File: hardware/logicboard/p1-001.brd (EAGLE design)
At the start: 47 x 72 mm, 24 parts, among them IC1 74LS07N

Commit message: OSHW logo.
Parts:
- added LOGO2: OSHW-LOGOL-COPPER, SparkFun-Aesthetics:OSHW-LOGO-L_COPPER
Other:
- board text removed: "/"
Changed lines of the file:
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@@
 <wire x1="16" y1="65" x2="16" y2="57" width="0.1524" layer="21"/>
 <wire x1="16" y1="57" x2="15" y2="57" width="0.1524" layer="21"/>
-<text x="6" y="61" size="5.08" layer="25" align="center">/</text>
 <text x="26.67" y="69.85" size="0.8128" layer="25" rot="R180" align="center">D4</text>
 <text x="29.21" y="69.85" size="0.8128" layer="25" rot="R180" align="center">D5</text>
@@
 <attribute name="VALUE" x="28.702" y="65.659" size="0.6096" layer="27" font="vector" ratio="20"/>
 </element>
+<element name="LOGO2" library="SparkFun-Aesthetics" package="OSHW-LOGO-L_COPPER" value="OSHW-LOGOL-COPPER" x="6" y="61"/>
 </elements>
 <signals>

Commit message: Pineapple logo v2.
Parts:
- removed LOGO2: OSHW-LOGOL-COPPER, SparkFun-Aesthetics:OSHW-LOGO-L_COPPER
- added LOGO1: OSHW-LOGOS-COPPER, SparkFun-Aesthetics:OSHW-LOGO-S_COPPER
- added U$2: PINEAPPLELOGO2, pineapplelogo2:PINEAPPLELOGO2
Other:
- board text removed: "Pineapple Design"
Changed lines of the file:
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@@
 <layers>
 <layer number="1" name="Top" color="4" fill="1" visible="yes" active="yes"/>
-<layer number="16" name="Bottom" color="1" fill="1" visible="yes" active="yes"/>
+<layer number="16" name="Bottom" color="1" fill="1" visible="no" active="yes"/>
 <layer number="17" name="Pads" color="2" fill="1" visible="yes" active="yes"/>
 <layer number="18" name="Vias" color="2" fill="1" visible="yes" active="yes"/>
@@
 <rectangle x1="0" y1="1" x2="1" y2="71" layer="41"/>
 <rectangle x1="0" y1="1" x2="1" y2="71" layer="42"/>
-<text x="6" y="67" size="1.27" layer="25">Pineapple Design</text>
 </plain>
 <attributes>
@@
 <attribute name="VALUE" x="28.702" y="65.659" size="0.6096" layer="27" font="vector" ratio="20"/>
 </element>
-<element name="LOGO2" library="SparkFun-Aesthetics" package="OSHW-LOGO-L_COPPER" value="OSHW-LOGOL-COPPER" x="6" y="61"/>
+<element name="LOGO1" library="SparkFun-Aesthetics" package="OSHW-LOGO-S_COPPER" value="OSHW-LOGOS-COPPER" x="6" y="60"/>
+<element name="U$2" library="pineapplelogo2" package="PINEAPPLELOGO2" value="PINEAPPLELOGO2" x="6" y="63"/>
 </elements>
 <signals>

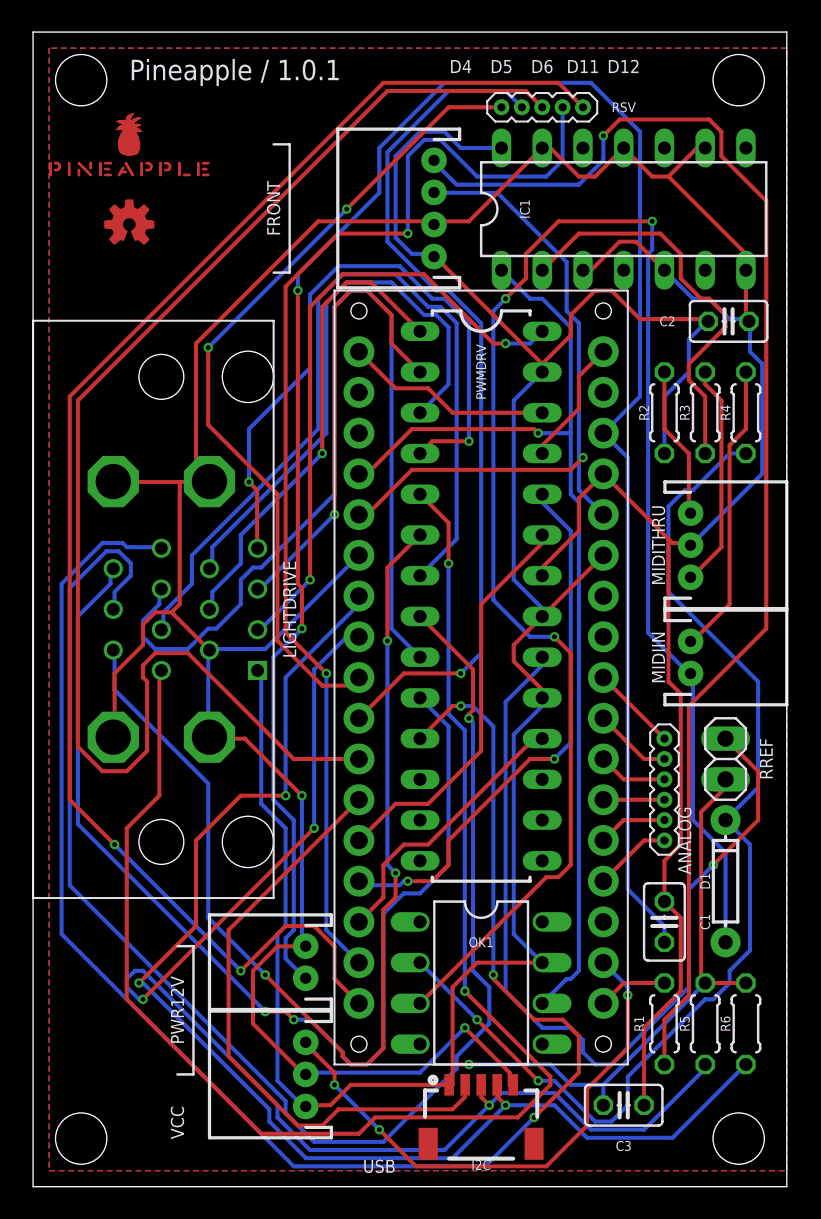
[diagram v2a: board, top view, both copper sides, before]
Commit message: New pineapple logo.
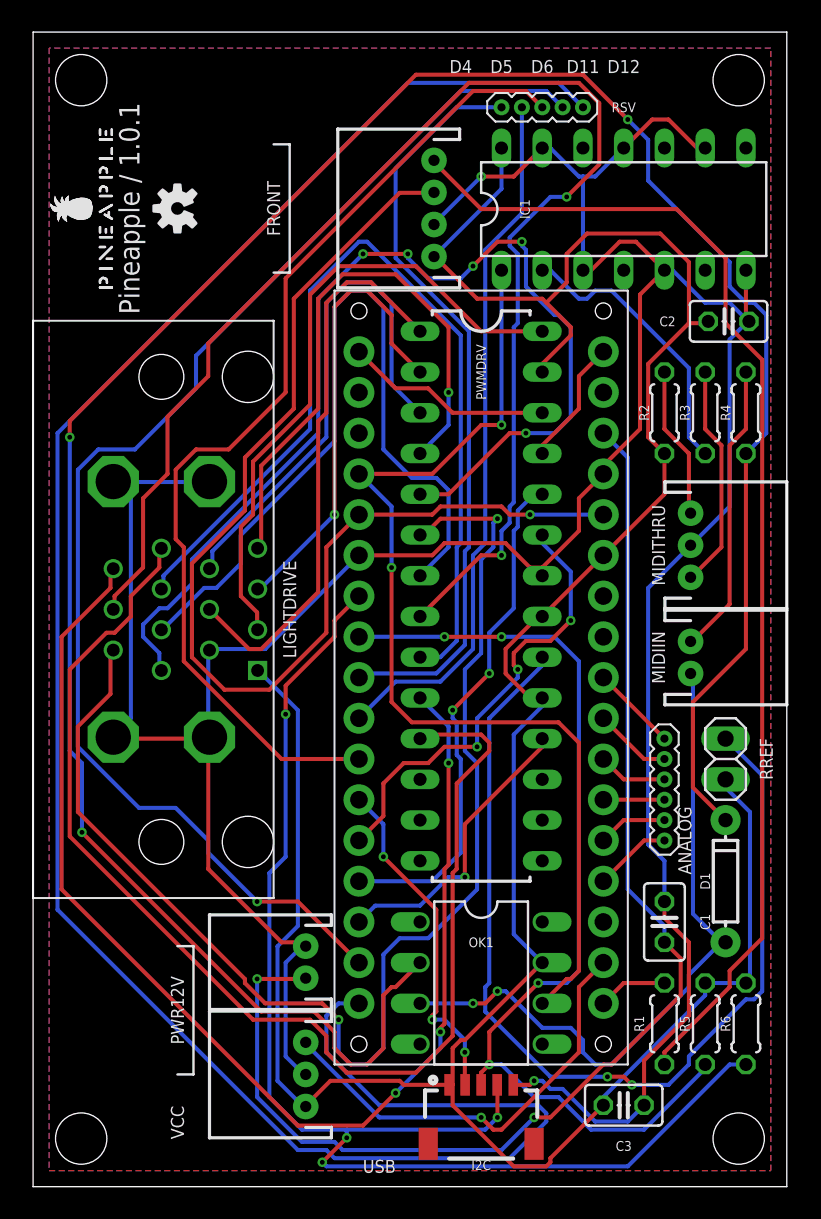
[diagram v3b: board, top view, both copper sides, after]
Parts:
- LOGO1: value OSHW-LOGOS-COPPER -> OSHW-LOGOS; device SparkFun-Aesthetics:OSHW-LOGO-S_COPPER -> SparkFun-Aesthetics:OSHW-LOGO-S
- U$2: value PINEAPPLELOGO2 -> PINEAPPLELOGO2SILKMINI; device pineapplelogo2:PINEAPPLELOGO2 -> pineapplelogo:PINEAPPLELOGO2SILKMINI
- moved LOGO1 3.16 mm to (9.00, 61.0), turned to 90 degrees
- moved U$2 2.24 mm to (5.00, 61.0), turned to 90 degrees
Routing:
- net N$5: track 68.3 -> 153.4 mm, vias 2 -> 3
- net MIDIIN-: track 110.6 -> 43.1 mm, vias 3 -> 2
- net VDD: track 128.3 -> 79.2 mm
- net D12: track 92.7 -> 130.4 mm, vias 2 -> 0
- net RST: track 42.5 -> 71.0 mm
- net LD6: track 92.7 -> 67.8 mm, vias 2 -> 5
- net LD12: track 100.7 -> 76.0 mm, vias 3 -> 0
- net D6: track 86.4 -> 62.8 mm
- net GND: track 231.9 -> 215.0 mm
- net SCL: track 77.6 -> 61.3 mm, vias 3 -> 4
- net D7: track 37.4 -> 21.2 mm, vias 0 -> 3
- net LD7: track 67.8 -> 81.2 mm, vias 3 -> 2
- net D5: track 53.8 -> 43.9 mm, vias 1 -> 0
- net D11: track 72.6 -> 82.4 mm, vias 2 -> 1
- net N$3: track 83.4 -> 74.5 mm, vias 1 -> 0
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
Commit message: Silk.
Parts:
- moved LOGO1 1.00 mm to (10.0, 61.0)
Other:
- board text added: "Pineapple I"
- board text added: "Rev. 1.0.1"
- board text removed: "Pineapple / 1.0.1"
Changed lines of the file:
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@@
 <hole x="44" y="69" drill="3.2"/>
 <hole x="3" y="69" drill="3.2"/>
-<text x="6" y="61" size="1.27" layer="25" rot="R90" align="center">Pineapple / 1.0.1</text>
+<text x="6" y="61" size="1.016" layer="25" rot="R90" align="center">Pineapple I</text>
 <hole x="20.32" y="8.89" drill="1"/>
 <hole x="35.56" y="8.89" drill="1"/>
@@
 <rectangle x1="46" y1="0" x2="47" y2="72" layer="41"/>
 <rectangle x1="46" y1="0" x2="47" y2="72" layer="42"/>
+<text x="7.5" y="61" size="1.016" layer="25" rot="R90" align="center">Rev. 1.0.1</text>
 </plain>
 <attributes>
@@
 <attribute name="VALUE" x="28.702" y="65.659" size="0.6096" layer="27" font="vector" ratio="20"/>
 </element>
-<element name="LOGO1" library="SparkFun-Aesthetics" package="OSHW-LOGO-S" value="OSHW-LOGOS" x="9" y="61" rot="R90"/>
+<element name="LOGO1" library="SparkFun-Aesthetics" package="OSHW-LOGO-S" value="OSHW-LOGOS" x="10" y="61" rot="R90"/>
 <element name="U$2" library="pineapplelogo" package="PINEAPPLELOGO2SILKMINI" value="PINEAPPLELOGO2SILKMINI" x="5" y="61" rot="R90"/>
 </elements>

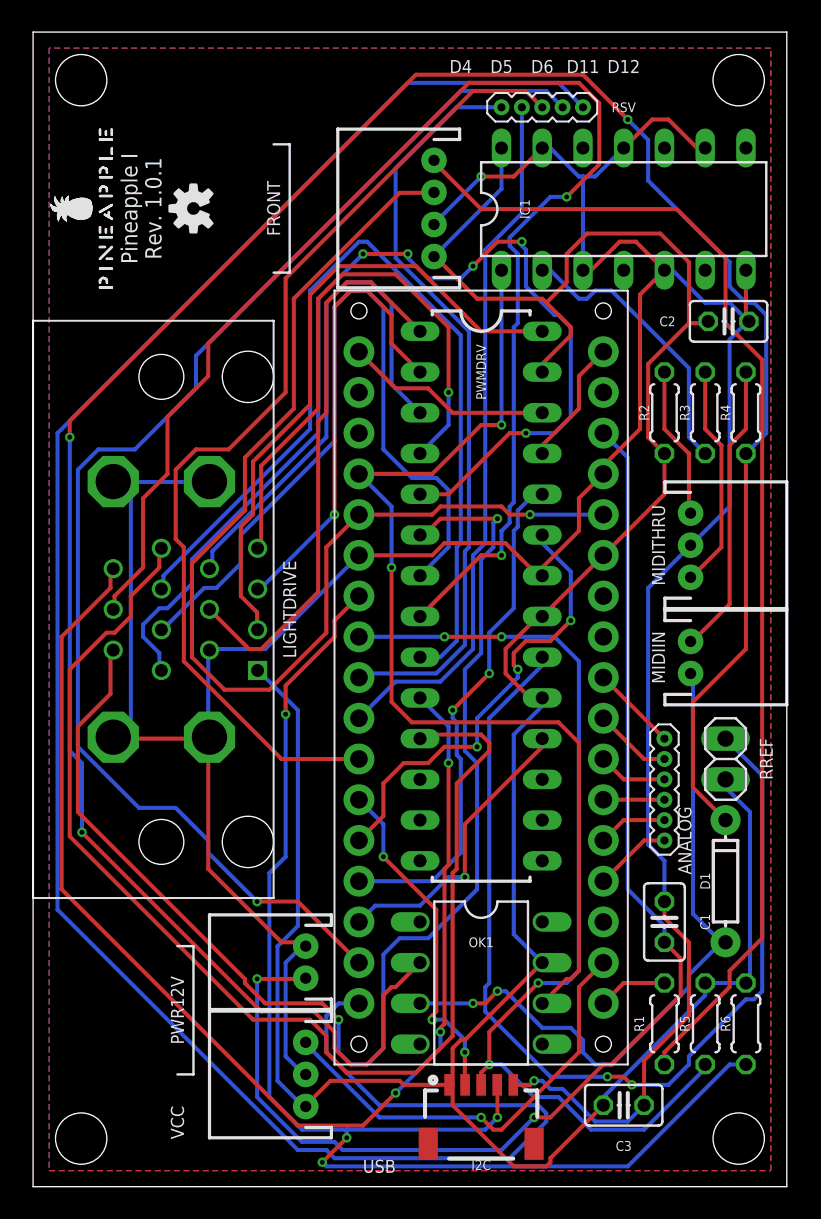
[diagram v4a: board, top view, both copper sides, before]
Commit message: Changed signal names.
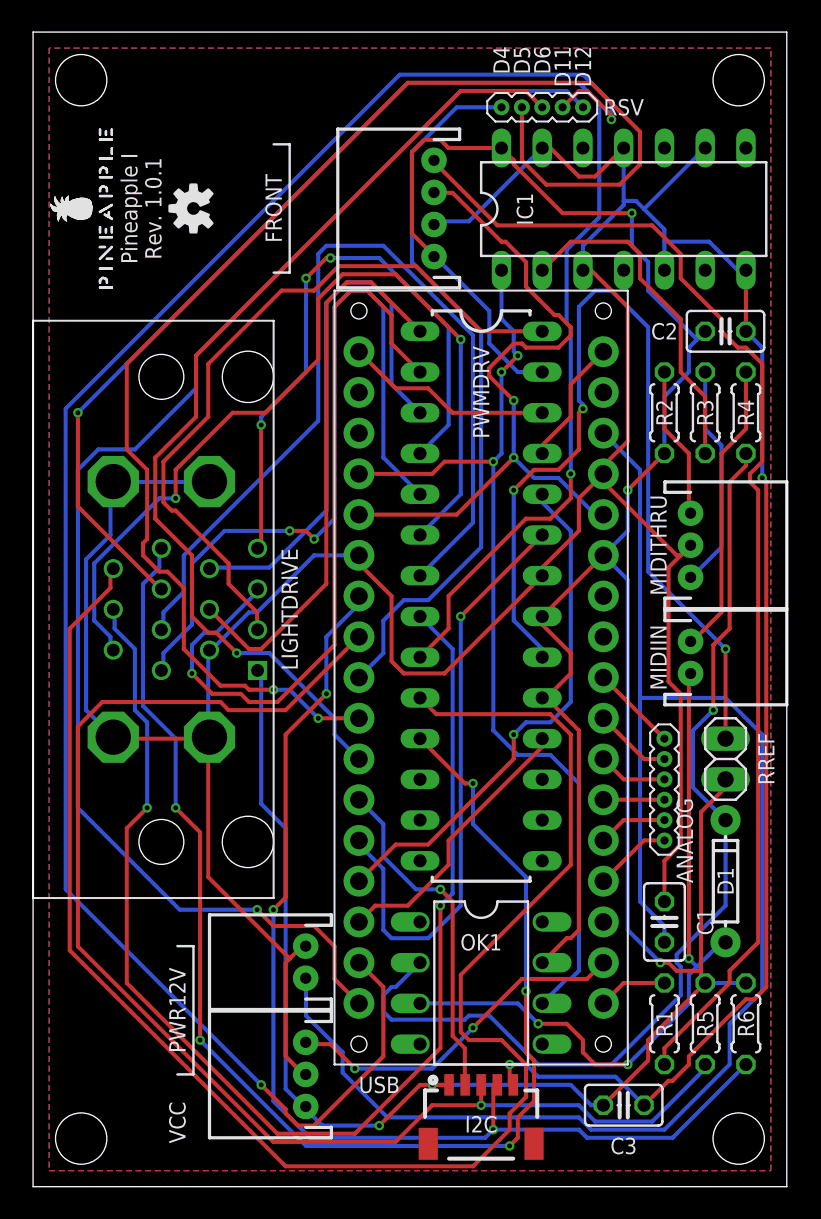
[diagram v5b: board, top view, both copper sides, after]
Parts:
- moved C2 0.65 mm to (43.2, 53.3)
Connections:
- net N$10 renamed A1
- net N$11 renamed A2
- net N$12 renamed A3
- net N$13 renamed A4
- net N$14 renamed A5
- net N$2 renamed N$MIDITHRU-RAW
- net N$3 renamed INDR
- net N$5 renamed MIDIINA
- net N$9 renamed A0
- net RX renamed MIDIIN
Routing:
- net MIDIINA: track 153.4 -> 63.4 mm, vias 3 -> 1
- net D5: track 43.9 -> 86.9 mm, vias 0 -> 2
- net D12: track 130.4 -> 87.7 mm, vias 0 -> 1
- net GND: track 215.0 -> 252.9 mm
- net LD10: track 57.4 -> 95.0 mm, vias 0 -> 2
- net D11: track 82.4 -> 113.1 mm, vias 1 -> 2
- net RST: track 71.0 -> 43.9 mm, vias 1 -> 2
- net LD7: track 81.2 -> 54.5 mm
- net LD11: track 75.8 -> 100.0 mm, vias 3 -> 0
- net SCL: track 61.3 -> 82.4 mm, vias 4 -> 1
- net LD6: track 67.8 -> 47.7 mm, vias 5 -> 2
- net LD3: track 28.6 -> 48.5 mm
- net VCC: track 178.4 -> 197.0 mm, vias 0 -> 5
- net VDD: track 79.2 -> 97.4 mm, vias 2 -> 0
- net SDA: track 82.8 -> 69.5 mm, vias 4 -> 3
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
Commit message: Version 1.0.1 -> 1.2.0.
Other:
- board text added: "Rev. 1.2.0"
- board text removed: "Rev. 1.0.1"
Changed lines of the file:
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@@
 <rectangle x1="46" y1="0" x2="47" y2="72" layer="41"/>
 <rectangle x1="46" y1="0" x2="47" y2="72" layer="42"/>
-<text x="7.5" y="61" size="1.016" layer="25" rot="R90" align="center">Rev. 1.0.1</text>
+<text x="7.5" y="61" size="1.016" layer="25" rot="R90" align="center">Rev. 1.2.0</text>
 </plain>
 <attributes>

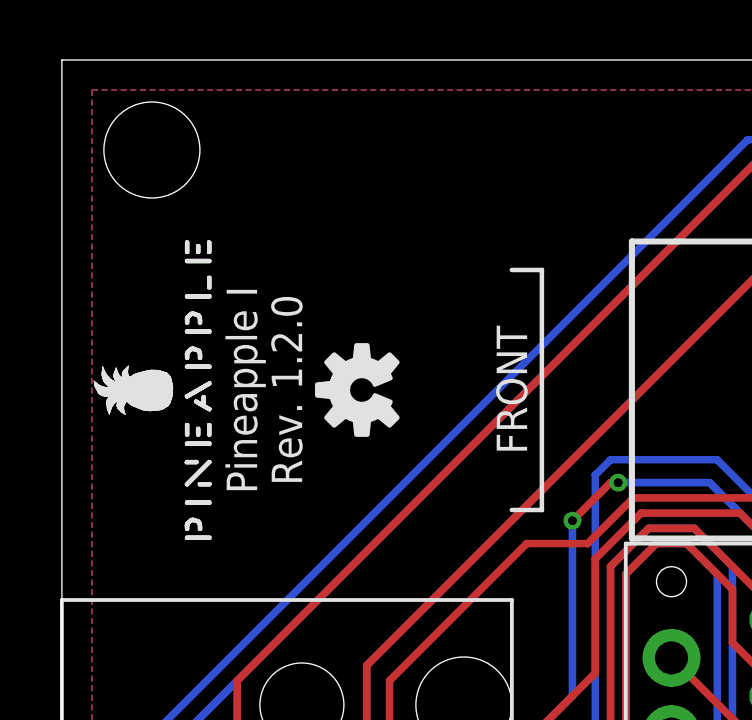
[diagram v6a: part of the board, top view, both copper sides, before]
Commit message: Pineapple Logo (vector->bitmap), OSHW logo (silk -> copper).
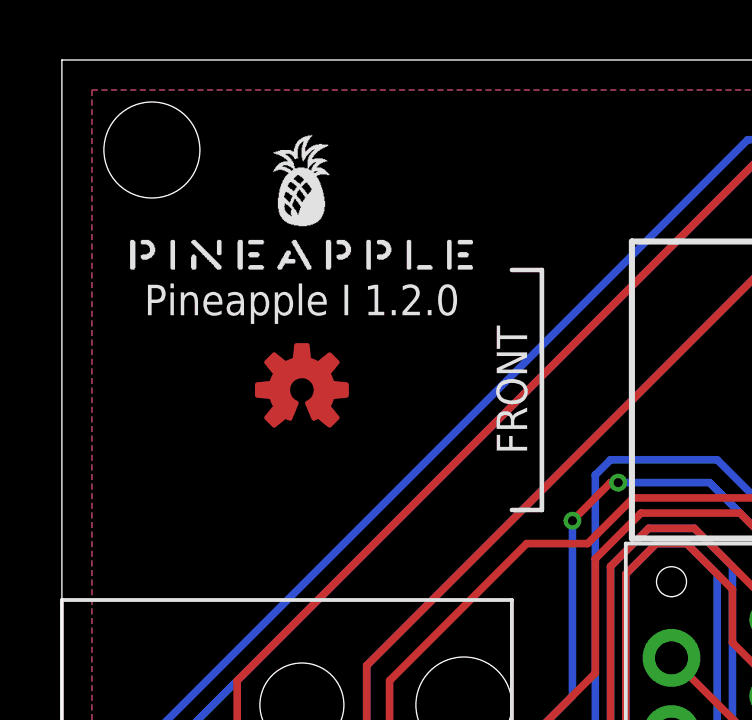
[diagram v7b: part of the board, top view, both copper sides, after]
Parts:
- LOGO1: value OSHW-LOGOS -> OSHW-LOGOS-COPPER; device SparkFun-Aesthetics:OSHW-LOGO-S -> SparkFun-Aesthetics:OSHW-LOGO-S_COPPER
- U$2: value PINEAPPLELOGO2SILKMINI -> PINEAPPLE450; device pineapplelogo:PINEAPPLELOGO2SILKMINI -> pineapple:PINEAPPLE450
- moved U$2 5.00 mm to (8.00, 65.0), turned to 0 degrees
- moved LOGO1 2.00 mm to (8.00, 61.0), turned to 0 degrees
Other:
- board text added: "Pineapple I 1.2.0"
- board text removed: "Pineapple I"
- board text removed: "Rev. 1.2.0"
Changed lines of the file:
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@@
 <hole x="44" y="69" drill="3.2"/>
 <hole x="3" y="69" drill="3.2"/>
-<text x="6" y="61" size="1.016" layer="25" rot="R90" align="center">Pineapple I</text>
+<text x="8" y="64" size="1.016" layer="25" align="center">Pineapple I 1.2.0</text>
 <hole x="20.32" y="8.89" drill="1"/>
 <hole x="35.56" y="8.89" drill="1"/>
@@
 <rectangle x1="46" y1="0" x2="47" y2="72" layer="41"/>
 <rectangle x1="46" y1="0" x2="47" y2="72" layer="42"/>
-<text x="7.5" y="61" size="1.016" layer="25" rot="R90" align="center">Rev. 1.2.0</text>
 </plain>
 <attributes>
@@
 <attribute name="VALUE" x="28.702" y="65.659" size="0.6096" layer="27" font="vector" ratio="20"/>
 </element>
-<element name="LOGO1" library="SparkFun-Aesthetics" package="OSHW-LOGO-S" value="OSHW-LOGOS" x="10" y="61" rot="R90"/>
-<element name="U$2" library="pineapplelogo" package="PINEAPPLELOGO2SILKMINI" value="PINEAPPLELOGO2SILKMINI" x="5" y="61" rot="R90"/>
+<element name="LOGO1" library="SparkFun-Aesthetics" package="OSHW-LOGO-S_COPPER" value="OSHW-LOGOS-COPPER" x="8" y="61"/>
+<element name="U$2" library="pineapple" package="PINEAPPLE450" value="PINEAPPLE450" x="8" y="65"/>
 </elements>
 <signals>
